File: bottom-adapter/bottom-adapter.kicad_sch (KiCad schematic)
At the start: 31 parts, among them J1 Solar Cell, J2 Burn Wire

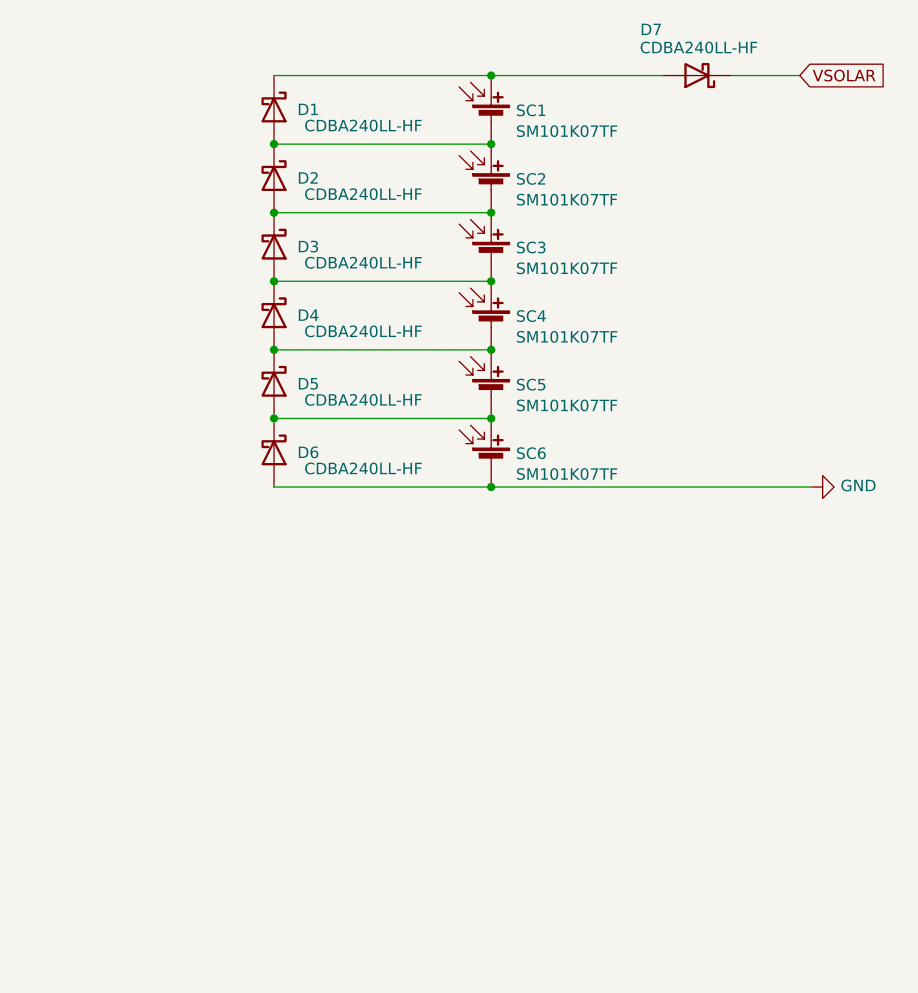
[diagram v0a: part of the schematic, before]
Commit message: fixed bottom adapter to be 3s2p
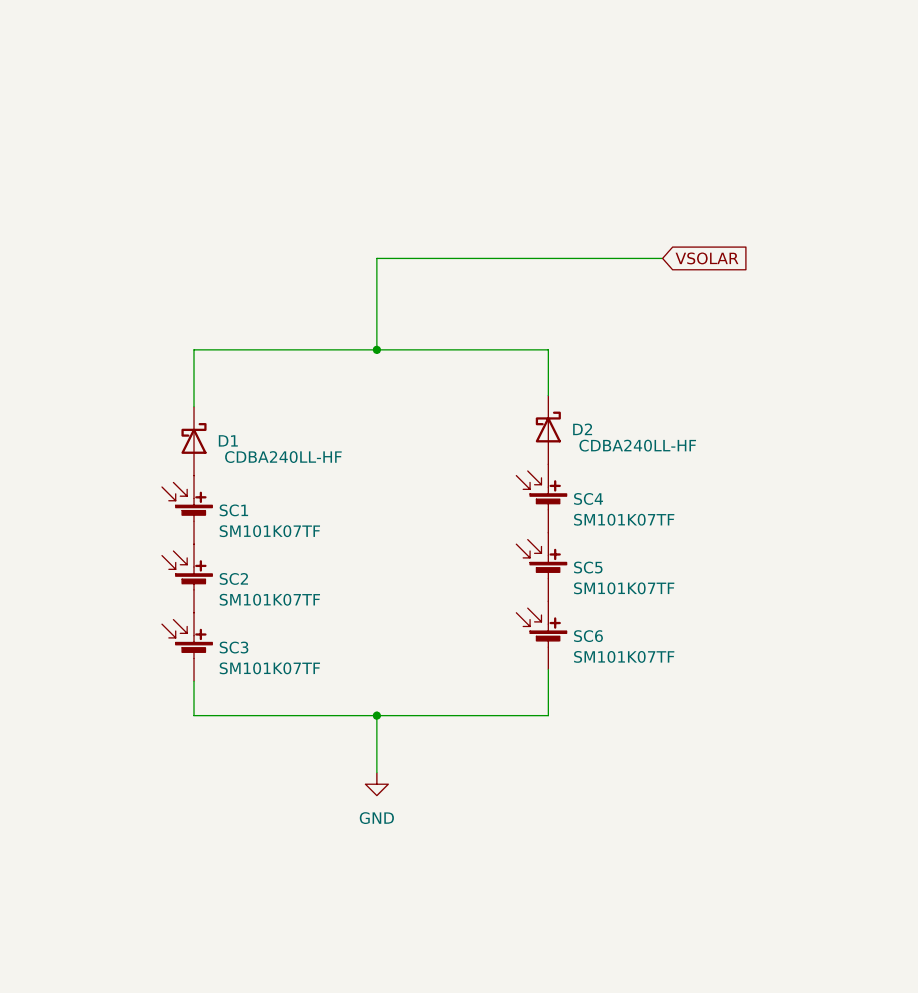
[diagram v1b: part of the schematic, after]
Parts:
- removed D3, D4, D5, D6, D7: CDBA240LL-HF, ISP:DO-214AC, symbol Device:D_Schottky
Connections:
- net GND: now also SC3.2 (-)
- net VSOLAR: now also D1.1 (K), D2.1 (K)
- net at SC1.2 (-), SC2.1 (+): no longer D1.2 (A), D2.1 (K)
- net at SC2.2 (-), SC3.1 (+): no longer D2.2 (A)
- net at SC4.1 (+): now also D2.2 (A); no longer SC3.2 (-)
- net at SC1.1 (+): now also D1.2 (A); no longer D1.1 (K)

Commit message: annotations
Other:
- title: bottom-adapter -> bottom-adapter-solar
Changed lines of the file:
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@@
   (paper "A4")
   (title_block
-    (title "bottom-adapter")
-    (date "2023-01-01")
-    (rev "1")
+    (title "bottom-adapter-solar")
+    (date "2023-01-03")
+    (rev "2")
   )
   (junction (at 167.64 63.5) (diameter 0) (color 0 0 0 0)
@@
   (symbol (lib_id "power:GND") (at 167.64 110.49 0) (unit 1)
     (in_bom yes) (on_board yes) (fields_autoplaced)
-    (property "Reference" "#PWR?" (id 0) (at 167.64 116.84 0)
+    (property "Reference" "#PWR0103" (id 0) (at 167.64 116.84 0)
       (effects (font (size 1.27 1.27)) hide)
     )
@@
       (reference "#PWR0102") (unit 1) (value "GND") (footprint "")
     )
+    (path "/ab97db33-d37d-4067-aabd-e60384abe3e7"
+      (reference "#PWR0103") (unit 1) (value "GND") (footprint "")
+    )
     (path "/f870594d-5222-4d93-aa0e-6f8613145649"
       (reference "#PWR0104") (unit 1) (value "GND") (footprint "")
@@
       (reference "#PWR0107") (unit 1) (value "GND") (footprint "")
     )
-    (path "/ab97db33-d37d-4067-aabd-e60384abe3e7"
-      (reference "#PWR?") (unit 1) (value "GND") (footprint "")
-    )
     (path "/16547f43-2994-4bdd-acb7-ff7fb67af51b"

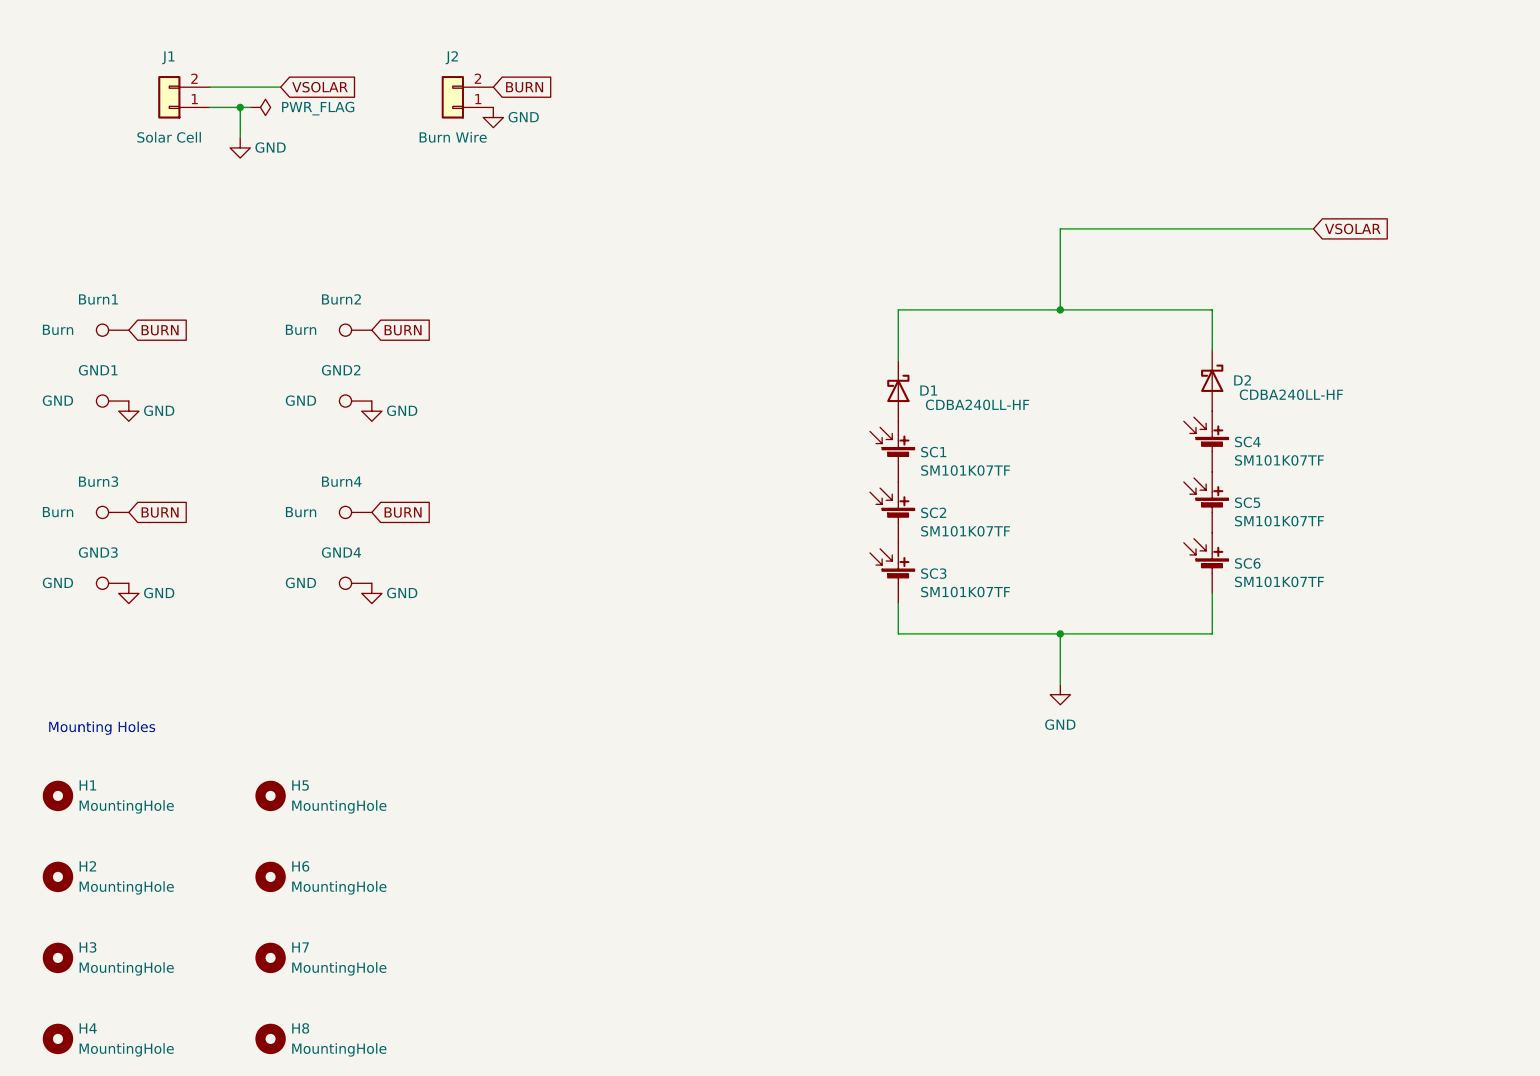
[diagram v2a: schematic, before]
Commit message: removed solar panels from bottom adapter and moved burn connector
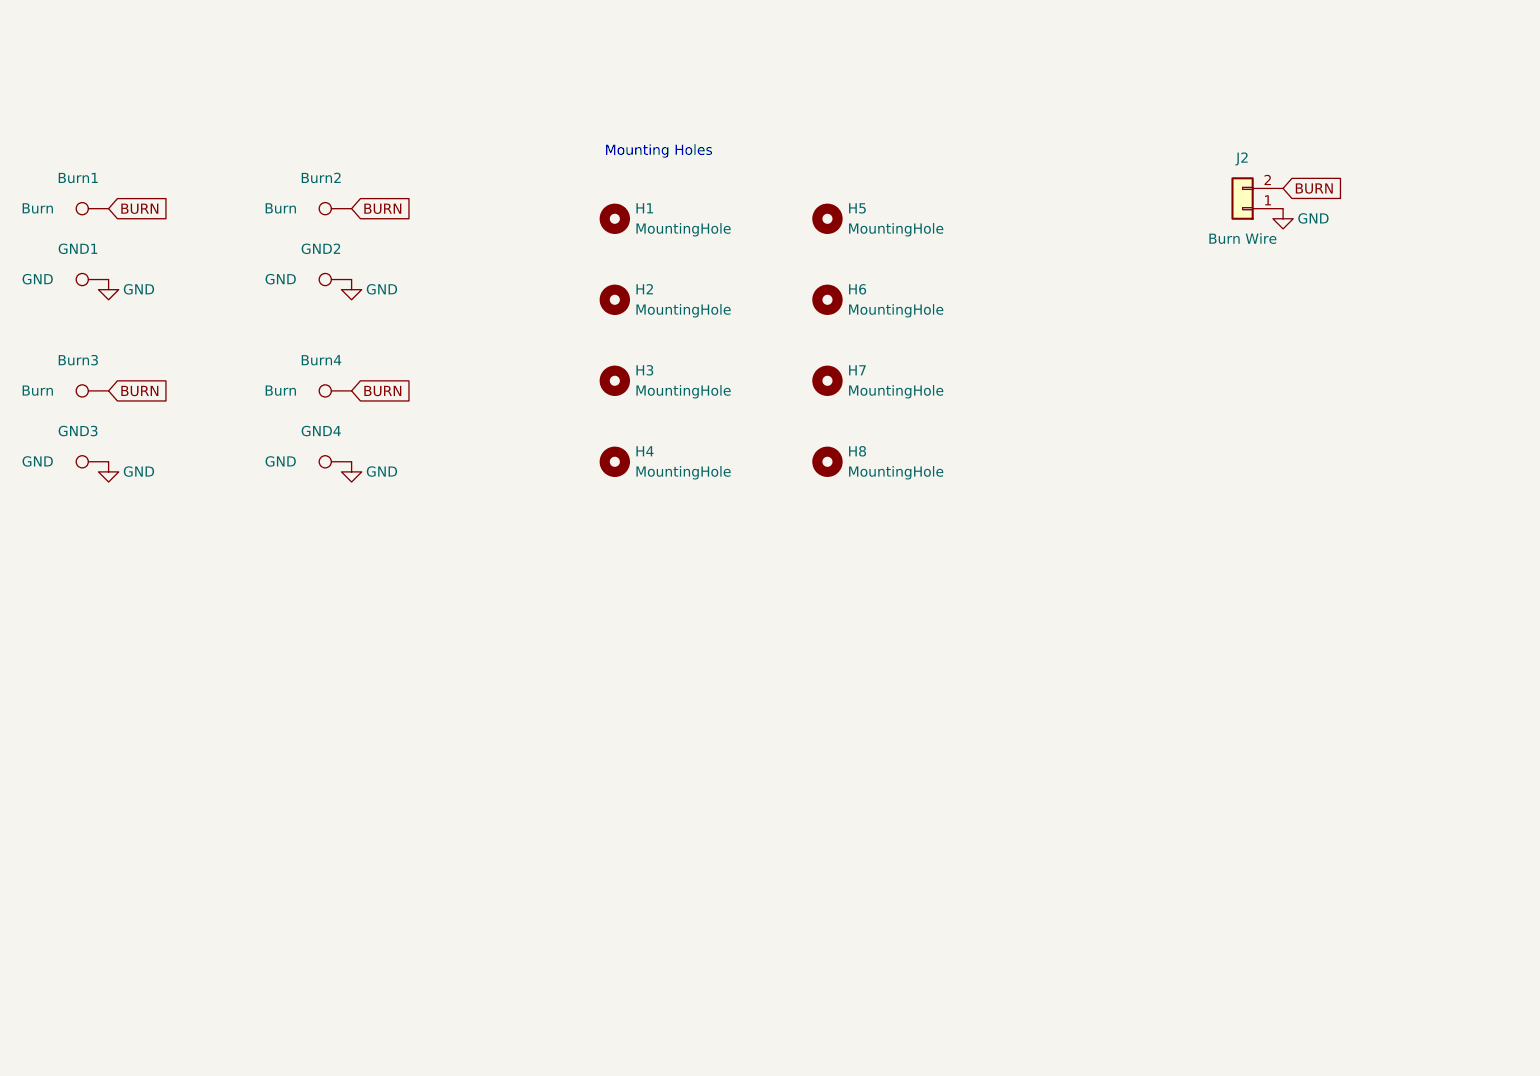
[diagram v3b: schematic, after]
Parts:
- removed D1, D2: CDBA240LL-HF, ISP:DO-214AC, symbol Device:D_Schottky
- removed J1: Solar Cell, ISP:pico_lock_2mm_2circuit, symbol Connector_Generic:Conn_01x02
- removed SC1, SC2, SC3, SC4, SC5, SC6: SM101K07TF, ISP:SM101K07TF, symbol Device:Solar_Cell
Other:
- title: bottom-adapter-solar -> bottom-adapter
- moved on the sheet: Burn1, Burn2, Burn3, Burn4, GND1, GND2, GND3, GND4, H1, H2, H3, H4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
